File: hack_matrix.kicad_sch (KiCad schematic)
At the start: 16 parts, among them J1 USB_C_Receptacle_USB2.0_16P, J2 Screw_Terminal_01x02, SW2 SW_Push, U1 SN74AHCT245PWR, U3 XC6206P332MR, U4 ESP32-S2-MINI-2, U5 SN74AHCT245PWR

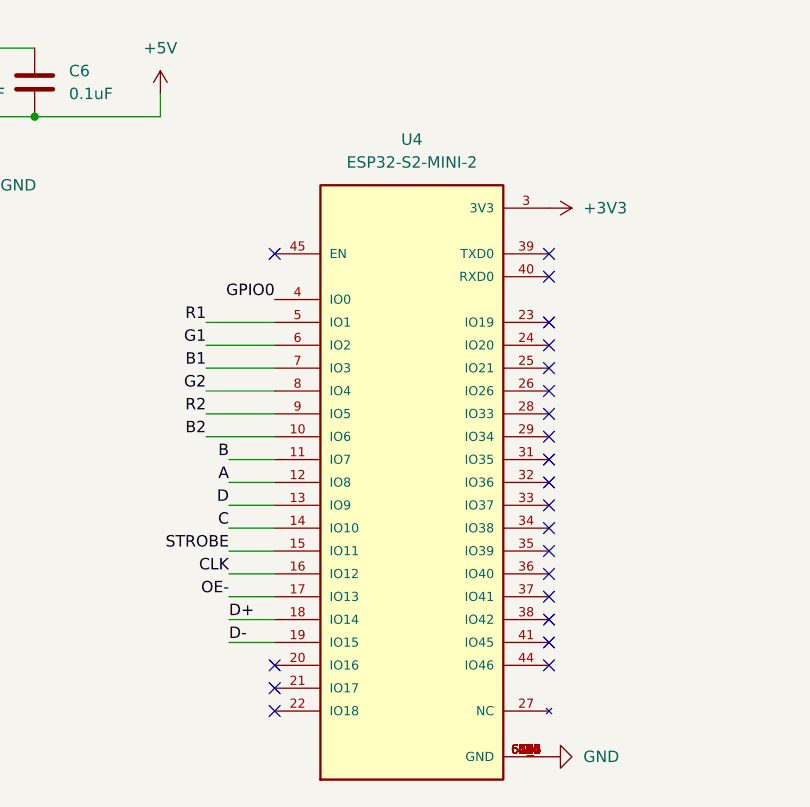
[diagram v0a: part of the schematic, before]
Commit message: update to fix USB wiring / EN pin.
TODO: fix screw jack part #
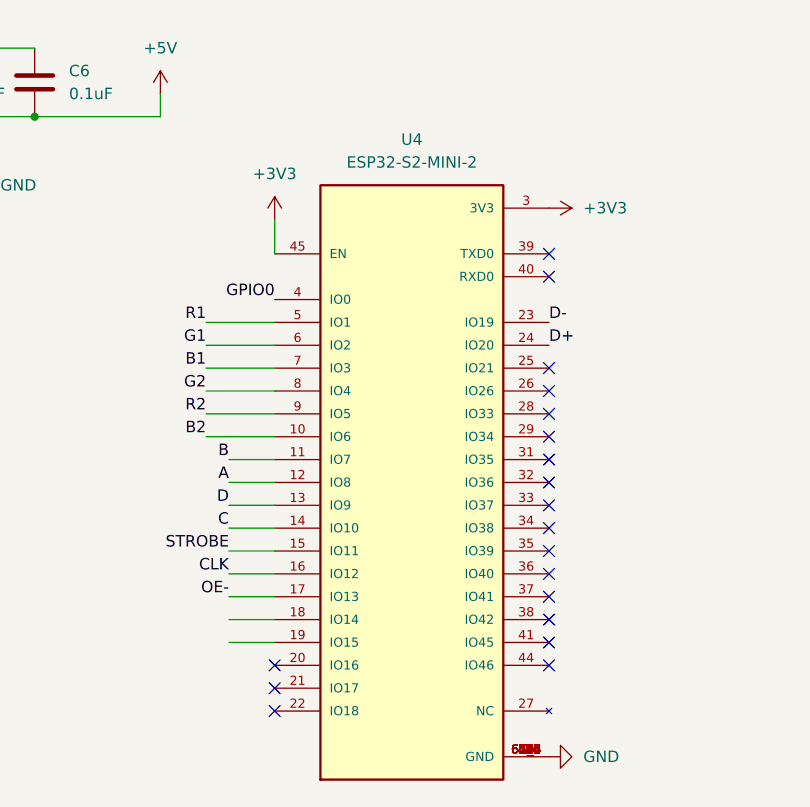
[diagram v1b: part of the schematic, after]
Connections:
- net +3V3: now also U4.45 (EN)
- net D+: now also U4.24 (IO20); no longer U4.18 (IO14)
- net D-: now also U4.23 (IO19); no longer U4.19 (IO15)
- no-connect marks 27 -> 24
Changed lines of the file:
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@@
 	)
 	(no_connect
-		(at 134.62 92.71)
-	)
-	(no_connect
 		(at 104.14 128.27)
 	)
@@
 	)
 	(no_connect
-		(at 134.62 90.17)
-	)
-	(no_connect
 		(at 134.62 95.25)
 	)
@@
 	)
 	(no_connect
-		(at 104.14 82.55)
-	)
-	(no_connect
 		(at 134.62 113.03)
 	)
@@
 	(wire
 		(pts
+			(xy 104.14 78.74) (xy 104.14 82.55)
+		)
+		(stroke
+			(width 0)
+			(type default)
+		)
+	)
+	(wire
+		(pts
 			(xy 219.71 148.59) (xy 219.71 121.92)
 		)
@@
 		)
 	)
+	(label "D-"
+		(at 134.62 90.17 0)
+		(fields_autoplaced yes)
+		(effects
+			(font
+				(size 1.27 1.27)
+			)
+			(justify left bottom)
+		)
+	)
 	(label "G1"
 		(at 180.34 90.17 180)
@@
 		)
 	)
-	(label "D+"
-		(at 99.06 123.19 0)
-		(fields_autoplaced yes)
-		(effects
-			(font
-				(size 1.27 1.27)
-			)
-			(justify left bottom)
-		)
-	)
 	(label "D"
 		(at 99.06 110.49 180)
@@
 		)
 	)
-	(label "D-"
-		(at 99.06 125.73 0)
-		(fields_autoplaced yes)
-		(effects
-			(font
-				(size 1.27 1.27)
-			)
-			(justify left bottom)
-		)
-	)
 	(label "C"
 		(at 99.06 113.03 180)
@@
 		)
 	)
+	(label "D+"
+		(at 134.62 92.71 0)
+		(fields_autoplaced yes)
+		(effects
+			(font
+				(size 1.27 1.27)
+			)
+			(justify left bottom)
+		)
+	)
 	(label "R2"
 		(at 180.34 97.79 180)
@@
 					(unit 1)
 				)
+			)
+		)
+	)
+	(symbol
+		(lib_id "power:+3V3")
+		(at 104.14 78.74 0)
+		(unit 1)
+		(exclude_from_sim no)
+		(in_bom yes)
+		(on_board yes)
+		(dnp no)
+		(fields_autoplaced yes)
+		(property "Reference" "#PWR012"
+			(at 104.14 82.55 0)
+			(effects
+				(font
+					(size 1.27 1.27)
+				)
+				(hide yes)
+			)
+		)
+		(property "Value" "+3V3"
+			(at 104.14 73.66 0)
+			(effects
+				(font
+					(size 1.27 1.27)
+				)
+			)
+		)
+		(property "Footprint" ""
+			(at 104.14 78.74 0)
+			(effects
+				(font
+					(size 1.27 1.27)
+				)
+				(hide yes)
+			)
+		)
+		(property "Datasheet" ""
+			(at 104.14 78.74 0)
+			(effects
+				(font
+					(size 1.27 1.27)
+				)
+				(hide yes)
+			)
+		)
+		(property "Description" "Power symbol creates a global label with name \"+3V3\""
+			(at 104.14 78.74 0)
+			(effects
+				(font
+					(size 1.27 1.27)
+				)
+				(hide yes)
+			)
+		)
+		(pin "1"
+		)
+		(instances
+			(project "hack_matrix"
+				(path "/f5b98ea7-14fe-45ed-a3b8-3726cfb4c1f2"
+					(reference "#PWR012")
+					(unit 1)
+				)
